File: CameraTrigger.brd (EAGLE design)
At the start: 68.6 x 53.3 mm, 29 parts, among them J1 3p-2.54, J2 3p-2.54, J3 3p-2.54, J4 3p-2.54, J5 3p-2.54, J6 3p-2.54, J7 3p-2.54, J8 3p-2.54, M1 ARDUINO_R3_ICSP, U2 PCF8574_PW_20, U3 DC-DC Switching, U4 MCP73831T-2ACI/OT

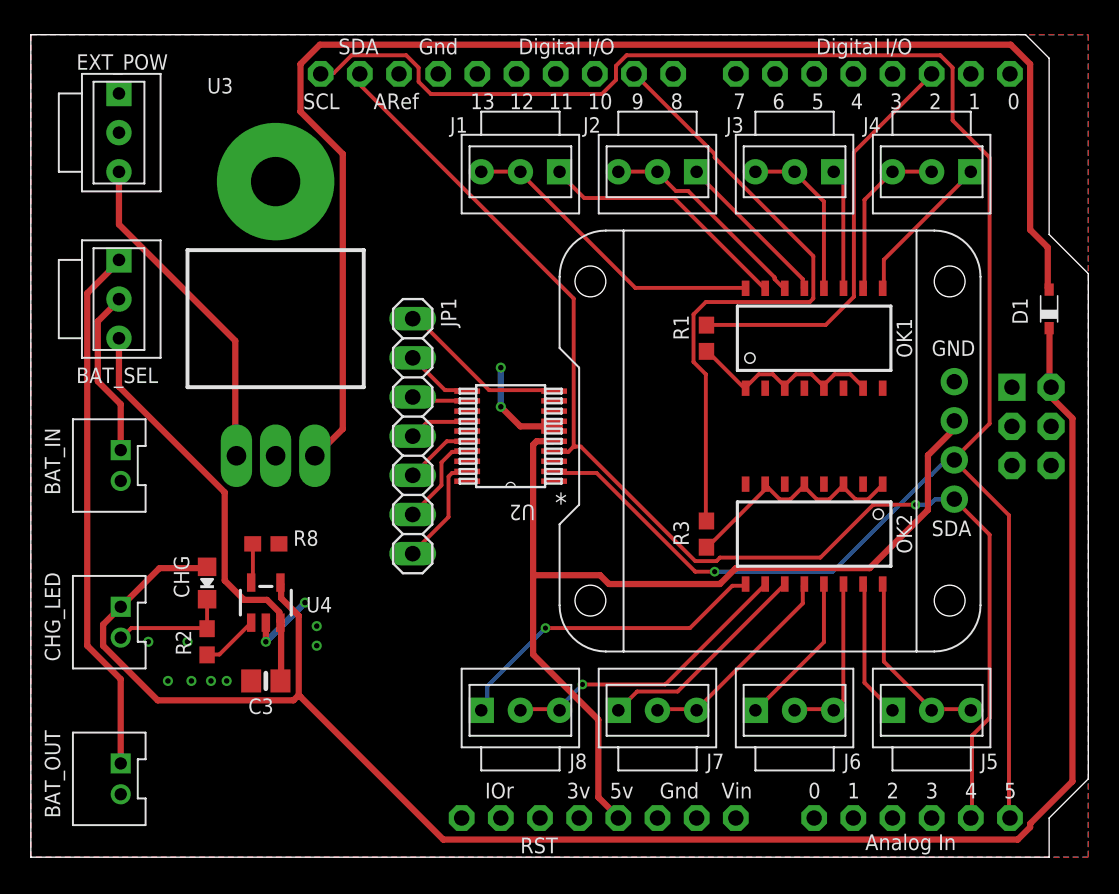
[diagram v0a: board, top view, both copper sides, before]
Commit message: Replace voltage regulator with DC-DC switchmode
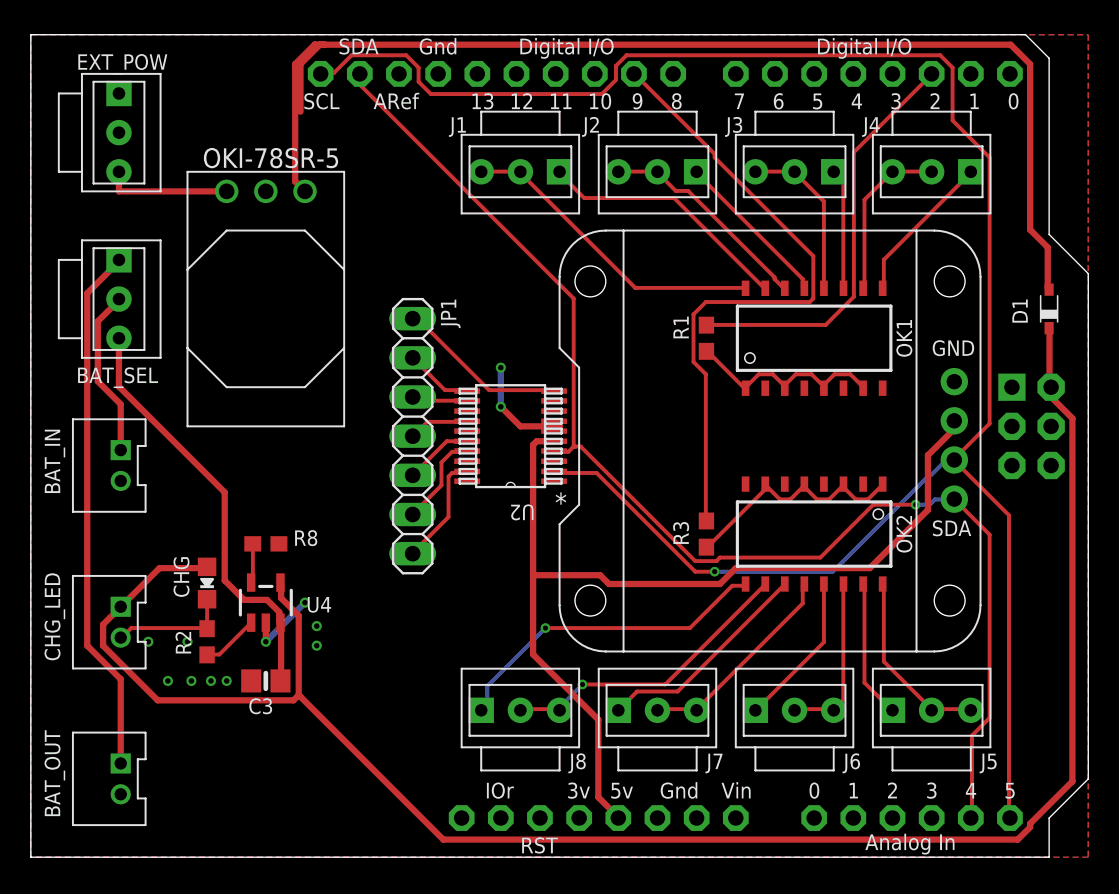
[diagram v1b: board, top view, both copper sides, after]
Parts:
- removed U3: DC-DC Switching, Seeed-OPL-ic:TO-220
- added OKI-78SR-5: DCDC_OKI-78SR, carrilib:OKI-78SRH
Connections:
- net GND: now also OKI-78SR-5.2; no longer U3.2, U3.HEAT
- net N$2: now also OKI-78SR-5.3; no longer U3.3
- net VEXT: now also OKI-78SR-5.1; no longer U3.1
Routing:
- net VEXT: track 21.6 -> 8.26 mm
- net N$2: track 90.8 -> 77.5 mm
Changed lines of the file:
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@@
 <attribute name="VALUE" x="21.59" y="36.195" size="1" layer="27" rot="R270"/>
-</element>
-<element name="U3" library="Seeed-OPL-ic" package="TO-220" value="DC-DC Switching" x="15.875" y="37.465" smashed="yes">
-<attribute name="MPN" value="L7805CV-DG" x="15.875" y="37.465" size="1.778" layer="27" display="off"/>
-<attribute name="NAME" x="11.43" y="49.53" size="1" layer="25" font="vector" ratio="21"/>
-<attribute name="VALUE" x="13.97" y="34.29" size="1" layer="27" ratio="11"/>
 </element>
 <element name="BAT_OUT" library="Seeed-OPL-Connector" package="H2-2.0-6X4.5MM" value="2p-2.0" x="5.08" y="5.08" smashed="yes" rot="R270">
@@
 <attribute name="VALUE" x="68.04" y="33.91" size="1" layer="27" rot="R90"/>
 </element>
+<element name="OKI-78SR-5" library="carrilib" package="OKI-78SRH" value="DCDC_OKI-78SR" x="15.24" y="43.18" smashed="yes" rot="R180">
+<attribute name="NAME" x="20.066" y="45.974" size="1.27" layer="25" rot="R180"/>
+</element>
 </elements>
 <signals>
 <signal name="VEXT" class="1">
-<contactref element="U3" pad="1"/>
 <contactref element="EXT_POW" pad="3"/>
-<wire x1="5.715" y1="41.0337" x2="5.715" y2="44.3484" width="0.4064" layer="1"/>
-<wire x1="13.2588" y1="33.4899" x2="5.715" y2="41.0337" width="0.4064" layer="1"/>
-<wire x1="13.2588" y1="26.0604" x2="13.2588" y2="33.4899" width="0.4064" layer="1"/>
-<wire x1="5.715" y1="44.3484" x2="5.715" y2="44.45" width="0.4064" layer="1"/>
-<wire x1="13.2588" y1="26.0604" x2="13.335" y2="26.035" width="0.4064" layer="1"/>
+<contactref element="OKI-78SR-5" pad="1"/>
+<wire x1="5.715" y1="43.18" x2="12.7" y2="43.18" width="0.4064" layer="1"/>
+<wire x1="5.715" y1="44.45" x2="5.715" y2="43.18" width="0.4064" layer="1"/>
 </signal>
 <signal name="D2">
@@
 <contactref element="U2" pad="9"/>
 <contactref element="U2" pad="15"/>
-<contactref element="U3" pad="HEAT"/>
-<contactref element="U3" pad="2"/>
 <contactref element="BAT_OUT" pad="-"/>
 <contactref element="BAT_IN" pad="-"/>
@@
 <via x="12.7" y="11.43" extent="1-16" drill="0.3556"/>
 <via x="10.414" y="11.43" extent="1-16" drill="0.3556"/>
+<contactref element="OKI-78SR-5" pad="2"/>
 </signal>
 <signal name="N$32">
@@
 </signal>
 <signal name="N$2" class="1">
-<contactref element="U3" pad="3"/>
 <contactref element="D1" pad="A"/>
 <wire x1="65.9511" y1="39.5478" x2="65.9511" y2="36.9189" width="0.4064" layer="1"/>
@@
 <wire x1="64.8081" y1="51.435" x2="64.8081" y2="40.6908" width="0.4064" layer="1"/>
 <wire x1="63.5508" y1="52.6923" x2="64.8081" y2="51.435" width="0.4064" layer="1"/>
-<wire x1="18.7452" y1="52.6923" x2="63.5508" y2="52.6923" width="0.4064" layer="1"/>
+<wire x1="18.7452" y1="52.6923" x2="19.05" y2="52.6923" width="0.4064" layer="1"/>
+<wire x1="19.05" y1="52.6923" x2="63.5508" y2="52.6923" width="0.4064" layer="1"/>
 <wire x1="17.4879" y1="51.435" x2="18.7452" y2="52.6923" width="0.4064" layer="1"/>
 <wire x1="17.4879" y1="48.3489" x2="17.4879" y2="51.435" width="0.4064" layer="1"/>
-<wire x1="20.2311" y1="45.6057" x2="17.4879" y2="48.3489" width="0.4064" layer="1"/>
-<wire x1="20.2311" y1="27.7749" x2="20.2311" y2="45.6057" width="0.4064" layer="1"/>
-<wire x1="18.5166" y1="26.0604" x2="20.2311" y2="27.7749" width="0.4064" layer="1"/>
 <wire x1="65.9511" y1="36.9189" x2="66.04" y2="36.81" width="0.4064" layer="1"/>
-<wire x1="18.5166" y1="26.0604" x2="18.415" y2="26.035" width="0.4064" layer="1"/>
+<contactref element="OKI-78SR-5" pad="3"/>
+<wire x1="17.145" y1="43.815" x2="17.78" y2="43.18" width="0.4064" layer="1"/>
+<wire x1="17.145" y1="51.435" x2="17.145" y2="43.815" width="0.4064" layer="1"/>
+<wire x1="18.415" y1="52.705" x2="17.145" y2="51.435" width="0.4064" layer="1"/>
+<wire x1="19.05" y1="52.705" x2="18.415" y2="52.705" width="0.4064" layer="1"/>
+<wire x1="19.05" y1="52.705" x2="19.05" y2="52.6923" width="0.4064" layer="1"/>
 </signal>
 </signals>
